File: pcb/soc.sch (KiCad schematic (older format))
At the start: 9 parts, among them J1 CC Debugger, Y1 32 Mhz

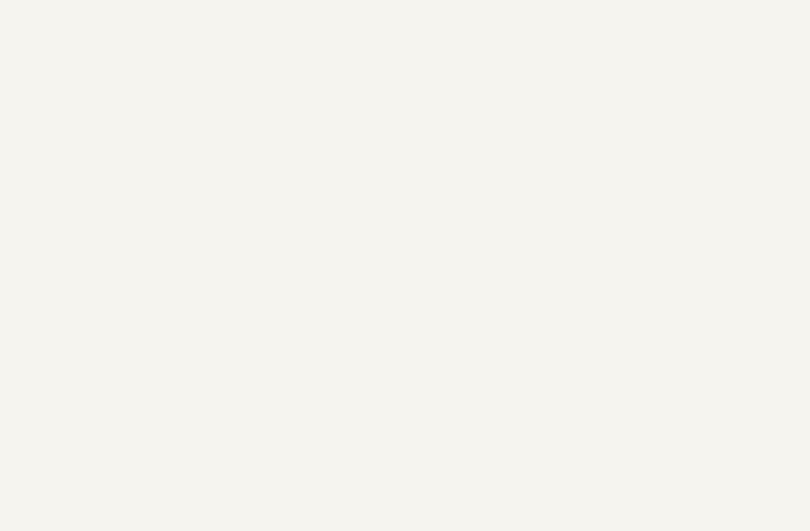
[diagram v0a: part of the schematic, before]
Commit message: Added hierarchical signals for E-Ink
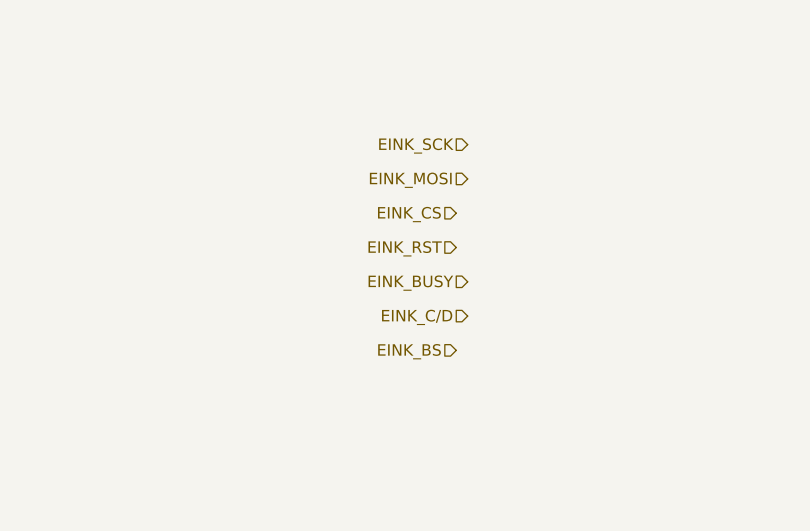
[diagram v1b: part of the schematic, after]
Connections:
- net labels added: EINK_BS, EINK_BUSY, EINK_C/D, EINK_CS, EINK_MOSI, EINK_RST, EINK_SCK
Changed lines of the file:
@@
 	1    0    0    -1
 $EndComp
+Text HLabel 1000 750  0    50   Input ~ 0
+EINK_SCK
+Text HLabel 1000 900  0    50   Input ~ 0
+EINK_MOSI
+Text HLabel 950  1050 0    50   Input ~ 0
+EINK_CS
+Text HLabel 950  1200 0    50   Input ~ 0
+EINK_RST
+Text HLabel 1000 1350 0    50   Input ~ 0
+EINK_BUSY
+Text HLabel 1000 1500 0    50   Input ~ 0
+EINK_C/D
+Text HLabel 950  1650 0    50   Input ~ 0
+EINK_BS
 $EndSCHEMATC

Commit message: Reverted to KiCad 4.0.7
+ Reworked debouncing for pushbuttons
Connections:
- wire segments 78 -> 70
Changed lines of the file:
@@
-EESchema Schematic File Version 4
+EESchema Schematic File Version 2
+LIBS:power
 LIBS:pir-cache
-EELAYER 26 0
+EELAYER 25 0
 EELAYER END
 $Descr A4 11693 8268
@@
 	-4450 2050 -4250 2050
 Wire Wire Line
-	-4250 2050 -4250 2450
+	-4250 2050 -4250 2750
 Wire Wire Line
 	-4250 2450 -4050 2450
@@
 	-4250 2750 -4050 2750
 Wire Wire Line
-	-2450 2750 -2350 2750
-Wire Wire Line
-	-2350 2550 -2350 2650
+	-2450 2750 -1750 2750
+Wire Wire Line
+	-2350 2550 -2350 3350
 Wire Wire Line
 	-2350 2650 -2450 2650
@@
 	-2450 3150 -1750 3150
 Wire Wire Line
-	-1750 3150 -1750 3750
+	-1750 3150 -1750 4050
 Wire Wire Line
 	-1750 3750 -1800 3750
@@
 	-2450 3250 -2150 3250
 Wire Wire Line
-	-2150 3250 -2150 3750
+	-2150 3250 -2150 4050
 Wire Wire Line
 	-2150 3750 -2100 3750
@@
 $EndComp
 Wire Wire Line
-	-2850 4150 -2850 4850
+	-2850 4150 -2850 5000
 Wire Wire Line
 	-2850 4850 -2750 4850
@@
 Wire Wire Line
 	-4050 3150 -4200 3150
-Wire Wire Line
-	-4250 2450 -4250 2750
-Wire Wire Line
-	-2350 2750 -1750 2750
-Wire Wire Line
-	-2350 2750 -2350 3050
-Wire Wire Line
-	-2350 2650 -2350 2750
-Wire Wire Line
-	-2350 3050 -2350 3350
-Wire Wire Line
-	-2150 3750 -2150 4050
-Wire Wire Line
-	-1750 3750 -1750 4050
-Wire Wire Line
-	-2850 4850 -2850 5000
 $Comp
 L stm32:STM32L051C6Tx U?

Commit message: MCU change, again
STM32L0 had quite a big problem, common reference for the comparators.
Another minus was the missing SWO for debugging.

STM32L4 has floating point, and most importantly, has embedded OPAMPS!
This means I can directly plug in the filter to the analog inputs and
everything is software. 2 opamps and 2 comparators (if needed).
External circuitry would be minimal for the PIR sensor.

It also means that I can read with the embedded 12-bit ADC the
amplified values. Precision is not crucial, we are interested in dips
and swells.
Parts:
- removed C21: 1μF, symbol device:C_Small
- removed C22: 1nF, symbol device:C_Small
- removed C23, C24: 12pF, symbol device:C_Small
- removed J1: CC Debugger, symbol conn:Conn_02x05_Odd_Even
- removed R3: 2.7K, symbol device:R
- removed R4: 56K, symbol device:R
- removed U?: STM32L051C6Tx, Housings_QFP:LQFP-48_7x7mm_Pitch0.5mm, symbol stm32:STM32L051C6Tx
- removed Y1: 32 Mhz, symbol device:Crystal
- added C? (x4): 12pF, symbol device:C_Small
- added C? (x2): 100nF, symbol device:C_Small
- added J?: SWD, symbol Conn_01x06_Male
- added J?: UART, symbol Conn_01x03_Male
- added JP?: Jumper_NC_Dual, symbol Jumper_NC_Dual
- added R?: 1K, symbol device:R
- added U?: STM32L476RETx, LQFP64, symbol STM32L476RETx
- added Y? (x2): 32 Mhz, symbol device:Crystal
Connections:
- net labels added: Debugger3V3, Down, EINK_D/C, EINK_PWR, Left, OK, PB0, PB1, PB2, RX, Right, SWCLK, SWDIO, SWO, TX, Up, nRESET
- net labels removed: Button, CC3V3, CSn, DC, DD, EINK_C/D, FOCUS, INTn, MISO, MOSI, PIR_HIGH, PIR_LOW, SCLK, SHUTTER
- wire segments 70 -> 75
- no-connect marks 10 -> 1
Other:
- note added: "Serial"

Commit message: Sensor logic implemented using MCU opamps
Of the ST PIR design I use the first 2 stages only, so no comparators.
1st stage using OPAMP1
2nd stage using OPAMP2

OPAMP1 amplifies the sensor output around the DC component of the PIR
sensor.

OPAMP2 amplifies the stage 1 output around half of VCC.

The output is then passed differentially to ADC which gives a
difference between stage 2 output and VCC/2.

This can be later converted into real volts by using the internal
VREFINT of the MCU because VCC can be measured against it. ST has
some (hopefully) cool factory calibration feature to compensate
for temperature deviations of the ADC which makes all this
possible  without external sigma-delta ADC.

The ADC has analog window thresholds that can be used to trigger
interrupts when input is beyond threshold. This means it is
possible to set sensitivity by modifying this threshold instead
of playing with the OPAMP2 gain (which anyway has only 4 levels).

(Just wasted a whole fucking saturday on this...)
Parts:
- added TP? (x18): TEST, symbol TEST
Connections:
- net labels added: Focus, OPAMP1+, OPAMP1-, OPAMP1OUT, OPAMP2+, OPAMP2-, OPAMP2OUT, Shutter, Type
- net labels removed: PB0, PB1, PB2
- wire segments 75 -> 98
- no-connect marks 1 -> 0

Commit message: Reworked the front diagram
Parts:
- removed TP?: TEST, symbol TEST
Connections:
- net labels added: Ambient
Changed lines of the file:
@@
 LIBS:ab2_usb
 LIBS:ab2_xtal
-LIBS:pir-cache
 EELAYER 25 0
 EELAYER END
 $Descr A3 16535 11693
 encoding utf-8
-Sheet 4 6
+Sheet 6 6
 Title ""
 Date ""
@@
 	0    1    1    0
 $EndComp
-$Comp
-L TEST TP?
-U 1 1 5A8433BD
-P 14750 5350
-F 0 "TP?" H 14750 5650 50  0000 C BNN
-F 1 "TEST" H 14750 5600 50  0000 C CNN
-F 2 "" H 14750 5350 50  0001 C CNN
-F 3 "" H 14750 5350 50  0001 C CNN
-	1    14750 5350
-	0    1    1    0
-$EndComp
 Wire Wire Line
 	14550 5350 14750 5350
@@
 Wire Wire Line
 	14550 4350 15550 4350
+Text HLabel 14750 5350 2    60   Input ~ 0
+Ambient
 $EndSCHEMATC

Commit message: Renamed all components
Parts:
- gave numbers to parts that had none: 30

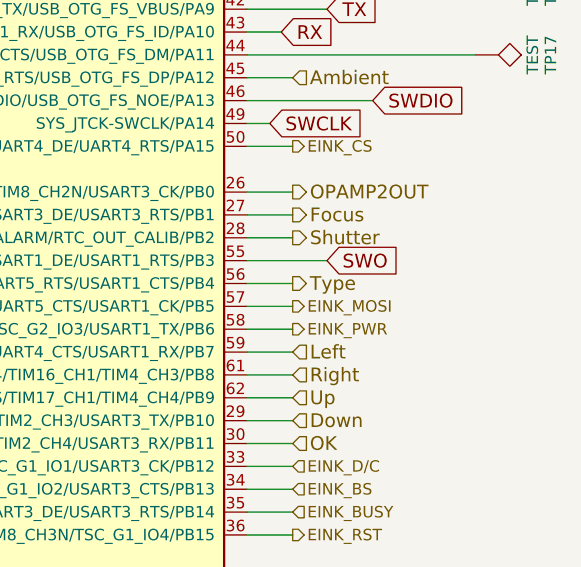
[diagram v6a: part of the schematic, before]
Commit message: Changed camera interface to use optocouplers
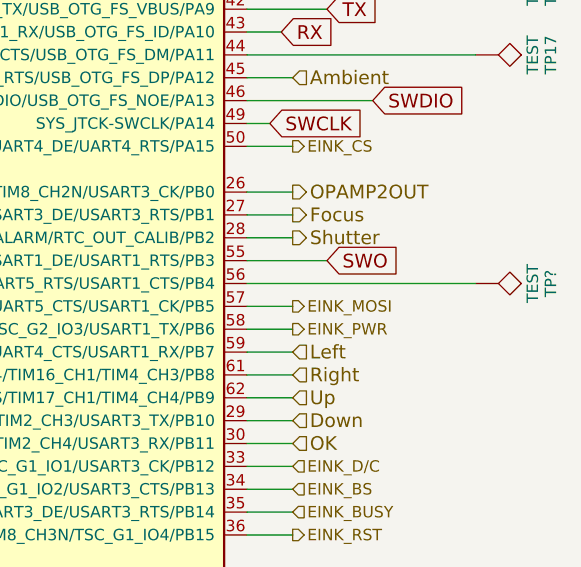
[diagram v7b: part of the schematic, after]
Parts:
- added TP?: TEST, symbol TEST
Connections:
- net labels removed: Type
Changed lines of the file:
@@
 LIBS:ab2_usb
 LIBS:ab2_xtal
+LIBS:EL817S
 LIBS:pir-cache
 EELAYER 25 0
@@
 EINK_PWR
 $Comp
-L power:Earth #PWR51
+L power:Earth #PWR53
 U 1 1 5A7F7482
 P 8800 3400
-F 0 "#PWR51" H 8800 3150 50  0001 C CNN
+F 0 "#PWR53" H 8800 3150 50  0001 C CNN
 F 1 "Earth" H 8800 3250 50  0001 C CNN
 F 2 "" H 8800 3400 50  0001 C CNN
@@
 $EndComp
 $Comp
-L power:VCC #PWR48
+L power:VCC #PWR50
 U 1 1 5A7F7645
 P 7850 3250
-F 0 "#PWR48" H 7850 3100 50  0001 C CNN
+F 0 "#PWR50" H 7850 3100 50  0001 C CNN
 F 1 "VCC" H 7850 3400 50  0000 C CNN
 F 2 "" H 7850 3250 50  0001 C CNN
@@
 $EndComp
 $Comp
-L power:Earth #PWR50
+L power:Earth #PWR52
 U 1 1 5A7F7940
 P 8400 7950
-F 0 "#PWR50" H 8400 7700 50  0001 C CNN
+F 0 "#PWR52" H 8400 7700 50  0001 C CNN
 F 1 "Earth" H 8400 7800 50  0001 C CNN
 F 2 "" H 8400 7950 50  0001 C CNN
@@
 $EndComp
 $Comp
-L power:Earth #PWR39
+L power:Earth #PWR41
 U 1 1 5A7F8695
 P 800 6400
-F 0 "#PWR39" H 800 6150 50  0001 C CNN
+F 0 "#PWR41" H 800 6150 50  0001 C CNN
 F 1 "Earth" H 800 6250 50  0001 C CNN
 F 2 "" H 800 6400 50  0001 C CNN
@@
 $EndComp
 $Comp
-L power:Earth #PWR40
+L power:Earth #PWR42
 U 1 1 5A7F869B
 P 1200 6400
-F 0 "#PWR40" H 1200 6150 50  0001 C CNN
+F 0 "#PWR42" H 1200 6150 50  0001 C CNN
 F 1 "Earth" H 1200 6250 50  0001 C CNN
 F 2 "" H 1200 6400 50  0001 C CNN
@@
 $EndComp
 $Comp
-L power:Earth #PWR42
+L power:Earth #PWR44
 U 1 1 5A7F8A34
 P 1500 8300
-F 0 "#PWR42" H 1500 8050 50  0001 C CNN
+F 0 "#PWR44" H 1500 8050 50  0001 C CNN
 F 1 "Earth" H 1500 8150 50  0001 C CNN
 F 2 "" H 1500 8300 50  0001 C CNN
@@
 $EndComp
 $Comp
-L power:Earth #PWR45
+L power:Earth #PWR47
 U 1 1 5A7F8A3A
 P 1900 8300
-F 0 "#PWR45" H 1900 8050 50  0001 C CNN
+F 0 "#PWR47" H 1900 8050 50  0001 C CNN
 F 1 "Earth" H 1900 8150 50  0001 C CNN
 F 2 "" H 1900 8300 50  0001 C CNN
@@
 $EndComp
 $Comp
-L power:Earth #PWR44
+L power:Earth #PWR46
 U 1 1 5A7F96B5
 P 1900 4050
-F 0 "#PWR44" H 1900 3800 50  0001 C CNN
+F 0 "#PWR46" H 1900 3800 50  0001 C CNN
 F 1 "Earth" H 1900 3900 50  0001 C CNN
 F 2 "" H 1900 4050 50  0001 C CNN
@@
 $EndComp
 $Comp
-L Earth #PWR41
+L Earth #PWR43
 U 1 1 5A7FA9BE
 P 1400 4200
-F 0 "#PWR41" H 1400 3950 50  0001 C CNN
+F 0 "#PWR43" H 1400 3950 50  0001 C CNN
 F 1 "Earth" H 1400 4050 50  0001 C CNN
 F 2 "" H 1400 4200 50  0001 C CNN
@@
 $EndComp
 $Comp
-L power:VCC #PWR38
+L power:VCC #PWR40
 U 1 1 5A7FAB49
 P 600 4150
-F 0 "#PWR38" H 600 4000 50  0001 C CNN
+F 0 "#PWR40" H 600 4000 50  0001 C CNN
 F 1 "VCC" H 600 4300 50  0000 C CNN
 F 2 "" H 600 4150 50  0001 C CNN
@@
 SWDIO
 $Comp
-L power:Earth #PWR43
+L power:Earth #PWR45
 U 1 1 5A7FC200
 P 1650 10100
-F 0 "#PWR43" H 1650 9850 50  0001 C CNN
+F 0 "#PWR45" H 1650 9850 50  0001 C CNN
 F 1 "Earth" H 1650 9950 50  0001 C CNN
 F 2 "" H 1650 10100 50  0001 C CNN
@@
 	3600 9950 3750 9950
 $Comp
-L power:Earth #PWR47
+L power:Earth #PWR49
 U 1 1 5A7FF0DB
 P 3900 10100
-F 0 "#PWR47" H 3900 9850 50  0001 C CNN
+F 0 "#PWR49" H 3900 9850 50  0001 C CNN
 F 1 "Earth" H 3900 9950 50  0001 C CNN
 F 2 "" H 3900 10100 50  0001 C CNN
@@
 	14750 6050 14550 6050
 $Comp
-L power:VCC #PWR46
+L power:VCC #PWR48
 U 1 1 5A8061D8
 P 2150 4550
-F 0 "#PWR46" H 2150 4400 50  0001 C CNN
+F 0 "#PWR48" H 2150 4400 50  0001 C CNN
 F 1 "VCC" H 2150 4700 50  0000 C CNN
 F 2 "" H 2150 4550 50  0001 C CNN
@@
 $EndComp
 $Comp
-L power:Earth #PWR49
+L power:Earth #PWR51
 U 1 1 5A806A82
 P 7850 3550
-F 0 "#PWR49" H 7850 3300 50  0001 C CNN
+F 0 "#PWR51" H 7850 3300 50  0001 C CNN
 F 1 "Earth" H 7850 3400 50  0001 C CNN
 F 2 "" H 7850 3550 50  0001 C CNN
@@
 Wire Wire Line
 	14550 7150 14750 7150
-Text HLabel 14750 6250 2    60   Output ~ 0
-Type
-Wire Wire Line
-	14550 6250 14750 6250
+Wire Wire Line
+	14550 6250 15550 6250
 Text HLabel 2350 8150 0    60   BiDi ~ 0
 SCL
@@
 Text HLabel 14750 5350 2    60   Input ~ 0
 Ambient
+$Comp
+L TEST TP?
+U 1 1 5A80E6EA
+P 15550 6250
+F 0 "TP?" H 15550 6550 50  0000 C BNN
+F 1 "TEST" H 15550 6500 50  0000 C CNN
+F 2 "" H 15550 6250 50  0001 C CNN
+F 3 "" H 15550 6250 50  0001 C CNN
+	1    15550 6250
+	0    1    1    0
+$EndComp
 $EndSCHEMATC

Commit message: Replaced original PIR symbol and ran ERC tests
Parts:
- gave numbers to parts that had none: 1
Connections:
- net labels removed: RESETn
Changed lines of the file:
@@
 LIBS:ab2_xtal
 LIBS:EL817S
+LIBS:IRA-S210ST01
 LIBS:pir-cache
 EELAYER 25 0
@@
 EINK_PWR
 $Comp
-L power:Earth #PWR53
+L power:Earth #PWR040
 U 1 1 5A7F7482
 P 8800 3400
-F 0 "#PWR53" H 8800 3150 50  0001 C CNN
+F 0 "#PWR040" H 8800 3150 50  0001 C CNN
 F 1 "Earth" H 8800 3250 50  0001 C CNN
 F 2 "" H 8800 3400 50  0001 C CNN
@@
 $EndComp
 $Comp
-L power:VCC #PWR50
+L power:VCC #PWR041
 U 1 1 5A7F7645
 P 7850 3250
-F 0 "#PWR50" H 7850 3100 50  0001 C CNN
+F 0 "#PWR041" H 7850 3100 50  0001 C CNN
 F 1 "VCC" H 7850 3400 50  0000 C CNN
 F 2 "" H 7850 3250 50  0001 C CNN
@@
 $EndComp
 $Comp
-L power:Earth #PWR52
+L power:Earth #PWR042
 U 1 1 5A7F7940
 P 8400 7950
-F 0 "#PWR52" H 8400 7700 50  0001 C CNN
+F 0 "#PWR042" H 8400 7700 50  0001 C CNN
 F 1 "Earth" H 8400 7800 50  0001 C CNN
 F 2 "" H 8400 7950 50  0001 C CNN
@@
 $EndComp
 $Comp
-L power:Earth #PWR41
+L power:Earth #PWR043
 U 1 1 5A7F8695
 P 800 6400
-F 0 "#PWR41" H 800 6150 50  0001 C CNN
+F 0 "#PWR043" H 800 6150 50  0001 C CNN
 F 1 "Earth" H 800 6250 50  0001 C CNN
 F 2 "" H 800 6400 50  0001 C CNN
@@
 $EndComp
 $Comp
-L power:Earth #PWR42
+L power:Earth #PWR044
 U 1 1 5A7F869B
 P 1200 6400
-F 0 "#PWR42" H 1200 6150 50  0001 C CNN
+F 0 "#PWR044" H 1200 6150 50  0001 C CNN
 F 1 "Earth" H 1200 6250 50  0001 C CNN
 F 2 "" H 1200 6400 50  0001 C CNN
@@
 $EndComp
 $Comp
-L power:Earth #PWR44
+L power:Earth #PWR045
 U 1 1 5A7F8A34
 P 1500 8300
-F 0 "#PWR44" H 1500 8050 50  0001 C CNN
+F 0 "#PWR045" H 1500 8050 50  0001 C CNN
 F 1 "Earth" H 1500 8150 50  0001 C CNN
 F 2 "" H 1500 8300 50  0001 C CNN
@@
 $EndComp
 $Comp
-L power:Earth #PWR47
+L power:Earth #PWR046
 U 1 1 5A7F8A3A
 P 1900 8300
-F 0 "#PWR47" H 1900 8050 50  0001 C CNN
+F 0 "#PWR046" H 1900 8050 50  0001 C CNN
 F 1 "Earth" H 1900 8150 50  0001 C CNN
 F 2 "" H 1900 8300 50  0001 C CNN
@@
 $EndComp
 Text GLabel 1200 3650 0    60   Input ~ 0
-RESETn
+nRESET
 $Comp
 L device:C_Small C38
@@
 $EndComp
 $Comp
-L power:Earth #PWR46
+L power:Earth #PWR047
 U 1 1 5A7F96B5
 P 1900 4050
-F 0 "#PWR46" H 1900 3800 50  0001 C CNN
+F 0 "#PWR047" H 1900 3800 50  0001 C CNN
 F 1 "Earth" H 1900 3900 50  0001 C CNN
 F 2 "" H 1900 4050 50  0001 C CNN
@@
 $EndComp
 $Comp
-L Earth #PWR43
+L Earth #PWR048
 U 1 1 5A7FA9BE
 P 1400 4200
-F 0 "#PWR43" H 1400 3950 50  0001 C CNN
+F 0 "#PWR048" H 1400 3950 50  0001 C CNN
 F 1 "Earth" H 1400 4050 50  0001 C CNN
 F 2 "" H 1400 4200 50  0001 C CNN
@@
 $EndComp
 $Comp
-L power:VCC #PWR40
+L power:VCC #PWR049
 U 1 1 5A7FAB49
 P 600 4150
-F 0 "#PWR40" H 600 4000 50  0001 C CNN
+F 0 "#PWR049" H 600 4000 50  0001 C CNN
 F 1 "VCC" H 600 4300 50  0000 C CNN
 F 2 "" H 600 4150 50  0001 C CNN
@@
 SWDIO
 $Comp
-L power:Earth #PWR45
+L power:Earth #PWR050
 U 1 1 5A7FC200
 P 1650 10100
-F 0 "#PWR45" H 1650 9850 50  0001 C CNN
+F 0 "#PWR050" H 1650 9850 50  0001 C CNN
 F 1 "Earth" H 1650 9950 50  0001 C CNN
 F 2 "" H 1650 10100 50  0001 C CNN
@@
 	3600 9950 3750 9950
 $Comp
-L power:Earth #PWR49
+L power:Earth #PWR051
 U 1 1 5A7FF0DB
 P 3900 10100
-F 0 "#PWR49" H 3900 9850 50  0001 C CNN
+F 0 "#PWR051" H 3900 9850 50  0001 C CNN
 F 1 "Earth" H 3900 9950 50  0001 C CNN
 F 2 "" H 3900 10100 50  0001 C CNN
@@
 	14750 6050 14550 6050
 $Comp
-L power:VCC #PWR48
+L power:VCC #PWR052
 U 1 1 5A8061D8
 P 2150 4550
-F 0 "#PWR48" H 2150 4400 50  0001 C CNN
+F 0 "#PWR052" H 2150 4400 50  0001 C CNN
 F 1 "VCC" H 2150 4700 50  0000 C CNN
 F 2 "" H 2150 4550 50  0001 C CNN
@@
 $EndComp
 $Comp
-L power:Earth #PWR51
+L power:Earth #PWR053
 U 1 1 5A806A82
 P 7850 3550
-F 0 "#PWR51" H 7850 3300 50  0001 C CNN
+F 0 "#PWR053" H 7850 3300 50  0001 C CNN
 F 1 "Earth" H 7850 3400 50  0001 C CNN
 F 2 "" H 7850 3550 50  0001 C CNN
@@
 Ambient
 $Comp
-L TEST TP?
+L TEST TP18
 U 1 1 5A80E6EA
 P 15550 6250
-F 0 "TP?" H 15550 6550 50  0000 C BNN
+F 0 "TP18" H 15550 6550 50  0000 C BNN
 F 1 "TEST" H 15550 6500 50  0000 C CNN
 F 2 "" H 15550 6250 50  0001 C CNN
